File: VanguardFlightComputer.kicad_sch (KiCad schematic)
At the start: 0 parts

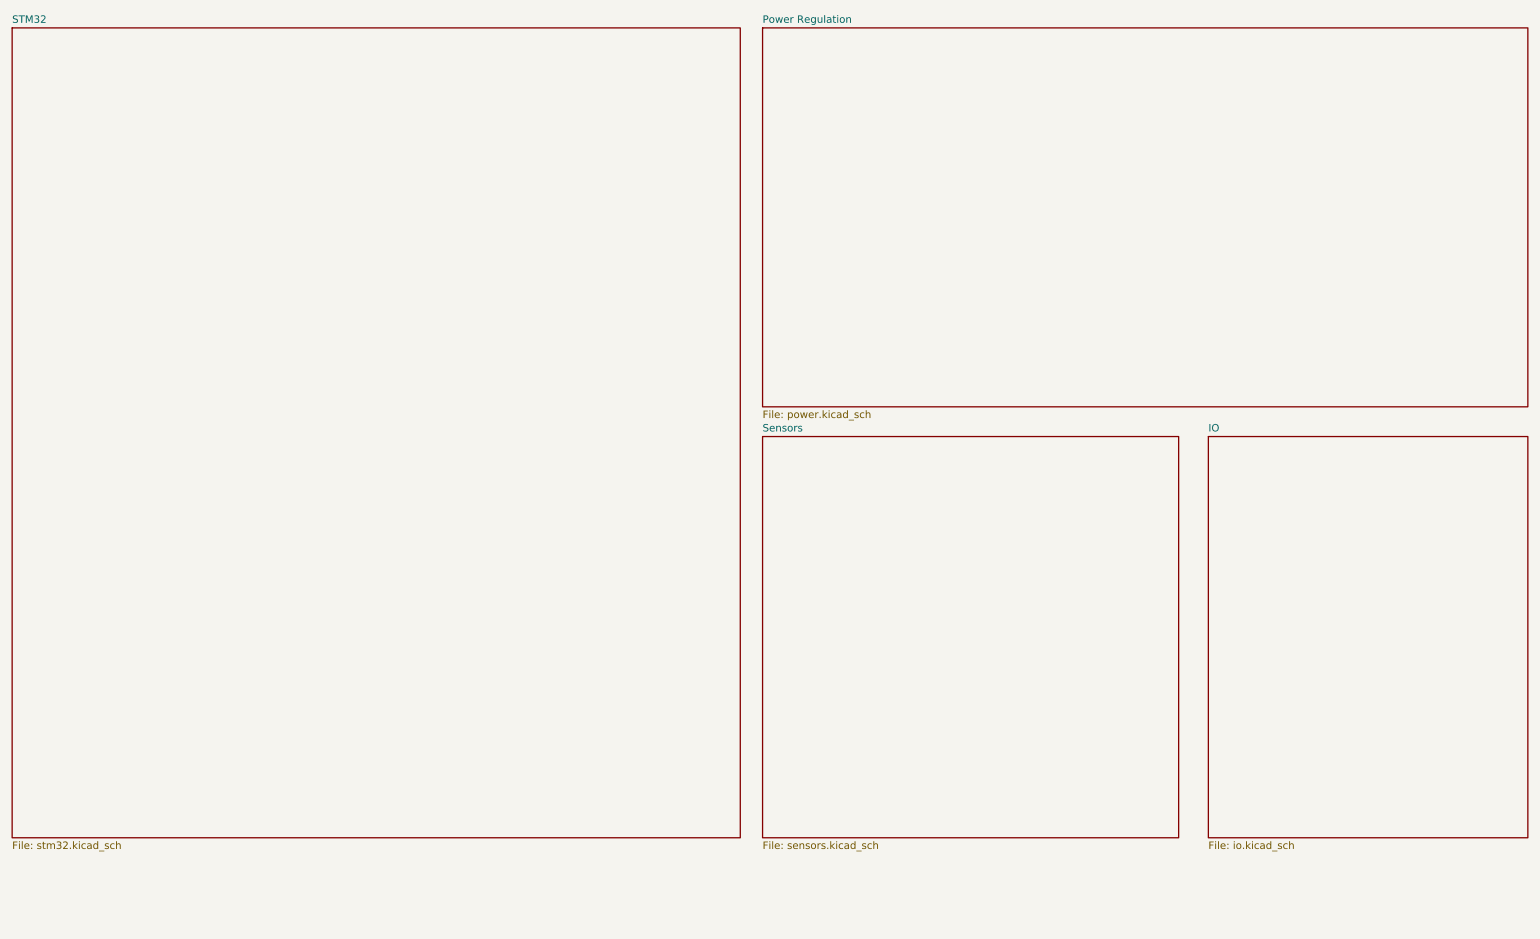
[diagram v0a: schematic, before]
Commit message: Added all sensors and telemetry modem
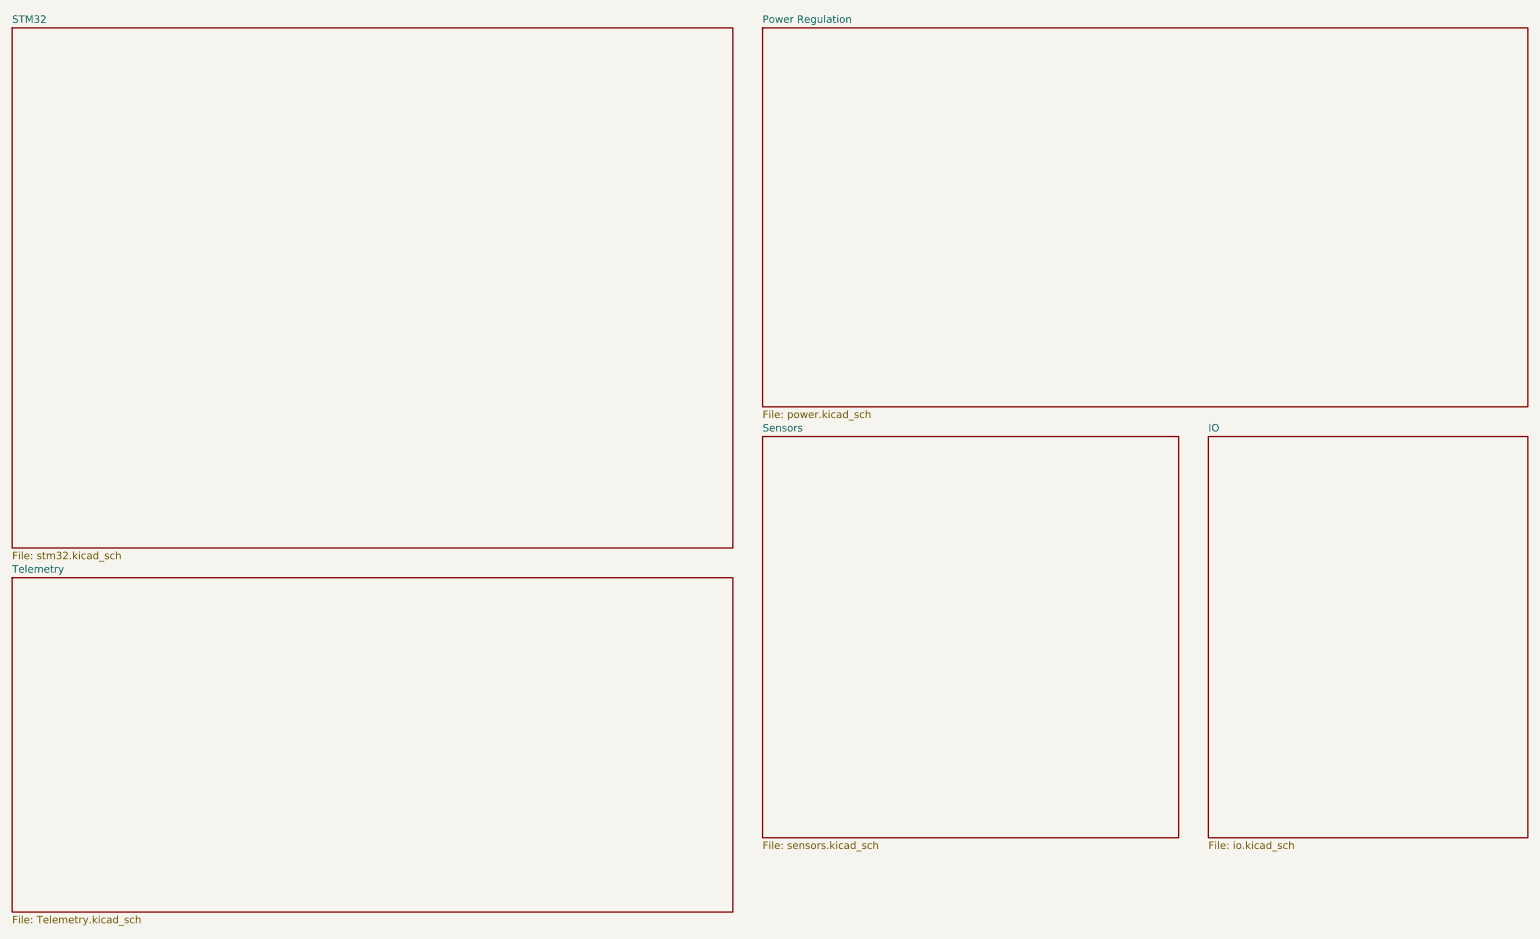
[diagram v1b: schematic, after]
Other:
- added sheet Telemetry (Telemetry.kicad_sch)
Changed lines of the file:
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@@
+	)
+	(sheet
+		(at 15.24 109.22)
+		(size 123.19 57.15)
+		(fields_autoplaced yes)
+		(stroke
+			(width 0.1524)
+			(type solid)
+		)
+		(fill
+			(color 0 0 0 0.0000)
+		)
+		(property "Sheetname" "Telemetry"
+			(at 15.24 108.5084 0)
+			(effects
+				(font
+					(size 1.27 1.27)
+				)
+				(justify left bottom)
+			)
+		)
+		(property "Sheetfile" "Telemetry.kicad_sch"
+			(at 15.24 166.9546 0)
+			(effects
+				(font
+					(size 1.27 1.27)
+				)
+				(justify left top)
+			)
+		)
+		(instances
+			(project "VanguardFlightComputer"
+				(path "/8210c139-a891-4d19-b6af-0ce30997a2bf"
+					(page "6")
+				)
+			)
+		)
 	)
 	(sheet
@@
 	(sheet
 		(at 15.24 15.24)
-		(size 124.46 138.43)
+		(size 123.19 88.9)
 		(fields_autoplaced yes)
 		(stroke
@@
 		)
 		(property "Sheetfile" "stm32.kicad_sch"
-			(at 15.24 154.2546 0)
+			(at 15.24 104.7246 0)
 			(effects
 				(font
